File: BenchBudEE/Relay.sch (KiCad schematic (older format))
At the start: 11 parts, among them K1 1461069-5, Q1 2N3904, U1 LTV-816S

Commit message: Layout Work Session 18
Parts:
- added TP4: RELAY_LOW, symbol CONN_1
- added TP?: 12P, symbol CONN_1
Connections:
- net +12P: now also TP?.1
- net at D2.1 (A), K1.5 (COIL-), Q1.3 (C): now also TP4.1
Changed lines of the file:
@@
 Sheet 5 9
 Title ""
-Date "18 mar 2014"
+Date "20 mar 2014"
 Rev ""
 Comp ""
@@
 	6500 1700 6500 1350
 $Comp
-L +12P #PWR038
+L +12P #PWR44
 U 1 1 52F63026
 P 6500 1350
-F 0 "#PWR038" H 6500 1320 30  0001 C CNN
+F 0 "#PWR44" H 6500 1320 30  0001 C CNN
 F 1 "+12P" H 6500 1450 30  0000 C CNN
 F 2 "" H 6500 1350 60  0000 C CNN
@@
 	7650 1750 7650 1400
 Wire Wire Line
-	7650 1400 6500 1400
+	6500 1400 7850 1400
 Connection ~ 6500 1400
 $Comp
-L GND_RELAY #PWR039
+L GND_RELAY #PWR45
 U 1 1 53133457
 P 8300 4800
-F 0 "#PWR039" H 8300 4800 30  0001 C CNN
+F 0 "#PWR45" H 8300 4800 30  0001 C CNN
 F 1 "GND_RELAY" H 8300 4730 30  0000 C CNN
 F 2 "" H 8300 4800 60  0000 C CNN
@@
 	1    0    0    -1
 $EndComp
+$Comp
+L CONN_1 TP4
+U 1 1 532B3F5C
+P 8600 3250
+F 0 "TP4" H 8680 3250 40  0000 L CNN
+F 1 "RELAY_LOW" H 8600 3305 30  0001 C CNN
+F 2 "" H 8600 3250 60  0000 C CNN
+F 3 "" H 8600 3250 60  0000 C CNN
+	1    8600 3250
+	1    0    0    -1
+$EndComp
+Connection ~ 7650 2500
+Wire Wire Line
+	8450 3250 8300 3250
+Connection ~ 8300 3250
+$Comp
+L CONN_1 TP?
+U 1 1 532B6892
+P 8000 1400
+F 0 "TP?" H 8080 1400 40  0000 L CNN
+F 1 "12P" H 8000 1455 30  0001 C CNN
+F 2 "" H 8000 1400 60  0000 C CNN
+F 3 "" H 8000 1400 60  0000 C CNN
+	1    8000 1400
+	1    0    0    -1
+$EndComp
+Connection ~ 7650 1400
 $EndSCHEMATC

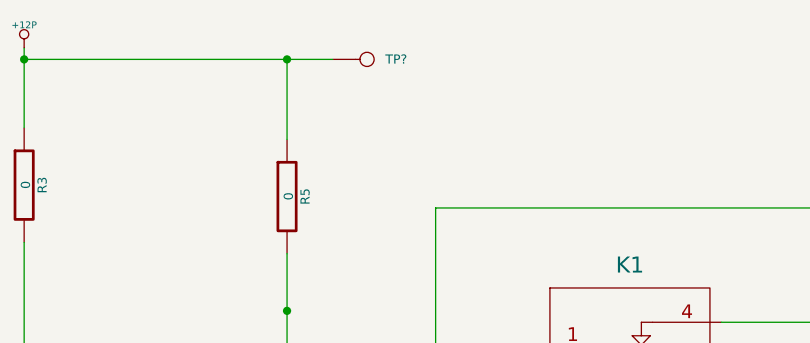
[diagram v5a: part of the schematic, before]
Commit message: Analog IO Cleanup/Additions
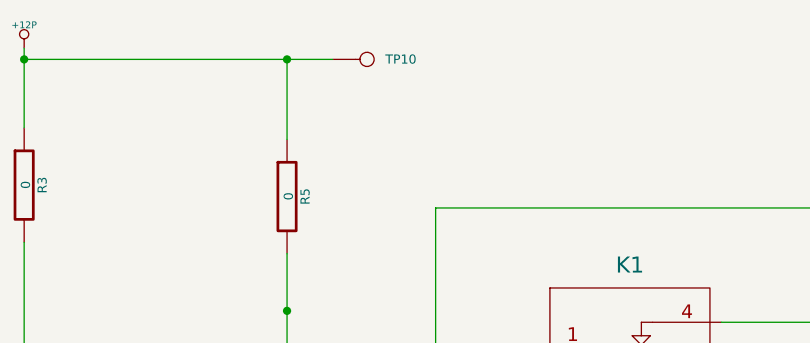
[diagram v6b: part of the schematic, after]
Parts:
- gave numbers to parts that had none: 1
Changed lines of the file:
@@
 Sheet 5 9
 Title ""
-Date "20 mar 2014"
+Date "26 mar 2014"
 Rev ""
 Comp ""
@@
 	6500 1700 6500 1350
 $Comp
-L +12P #PWR44
+L +12P #PWR037
 U 1 1 52F63026
 P 6500 1350
-F 0 "#PWR44" H 6500 1320 30  0001 C CNN
+F 0 "#PWR037" H 6500 1320 30  0001 C CNN
 F 1 "+12P" H 6500 1450 30  0000 C CNN
 F 2 "" H 6500 1350 60  0000 C CNN
@@
 Connection ~ 6500 1400
 $Comp
-L GND_RELAY #PWR45
+L GND_RELAY #PWR038
 U 1 1 53133457
 P 8300 4800
-F 0 "#PWR45" H 8300 4800 30  0001 C CNN
+F 0 "#PWR038" H 8300 4800 30  0001 C CNN
 F 1 "GND_RELAY" H 8300 4730 30  0000 C CNN
 F 2 "" H 8300 4800 60  0000 C CNN
@@
 Connection ~ 8300 3250
 $Comp
-L CONN_1 TP?
+L CONN_1 TP10
 U 1 1 532B6892
 P 8000 1400
-F 0 "TP?" H 8080 1400 40  0000 L CNN
+F 0 "TP10" H 8080 1400 40  0000 L CNN
 F 1 "12P" H 8000 1455 30  0001 C CNN
 F 2 "" H 8000 1400 60  0000 C CNN

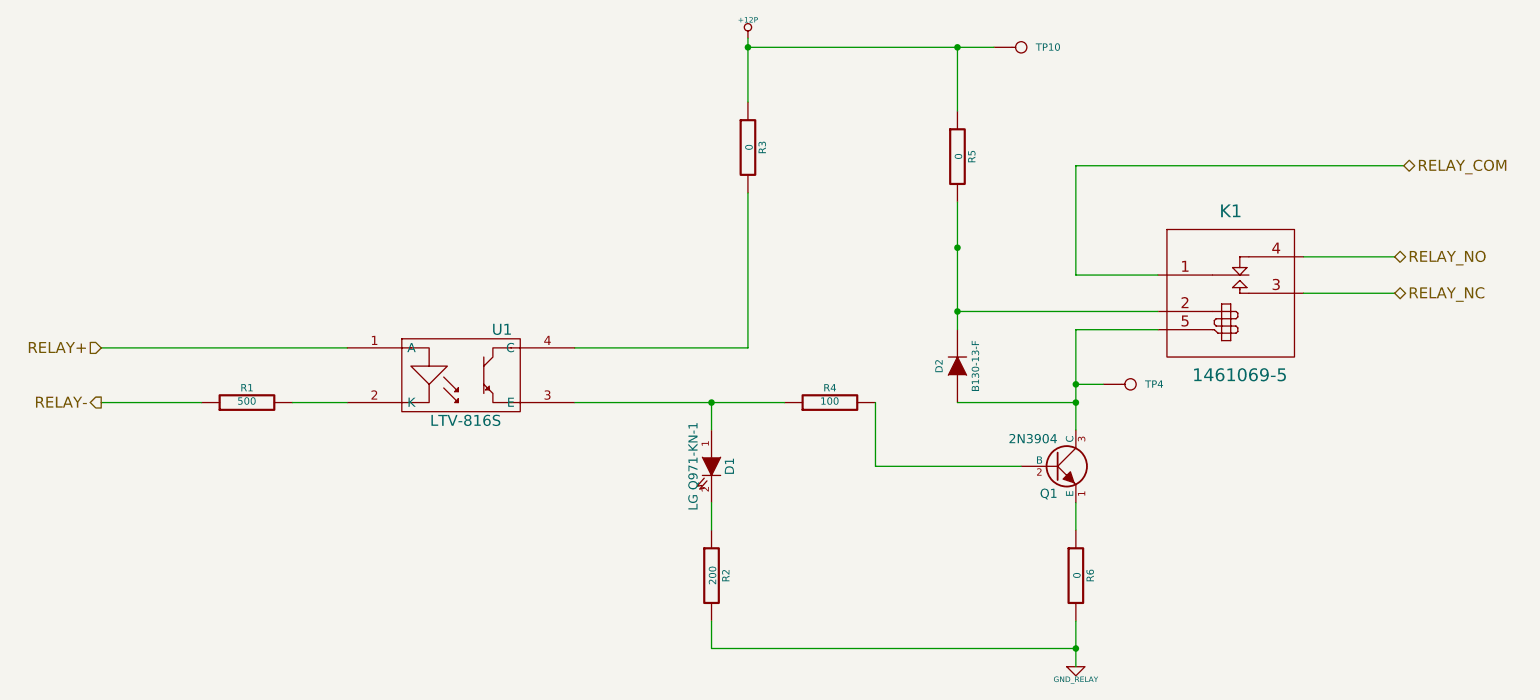
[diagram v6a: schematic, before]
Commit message: Changes for the BOM and BOMs
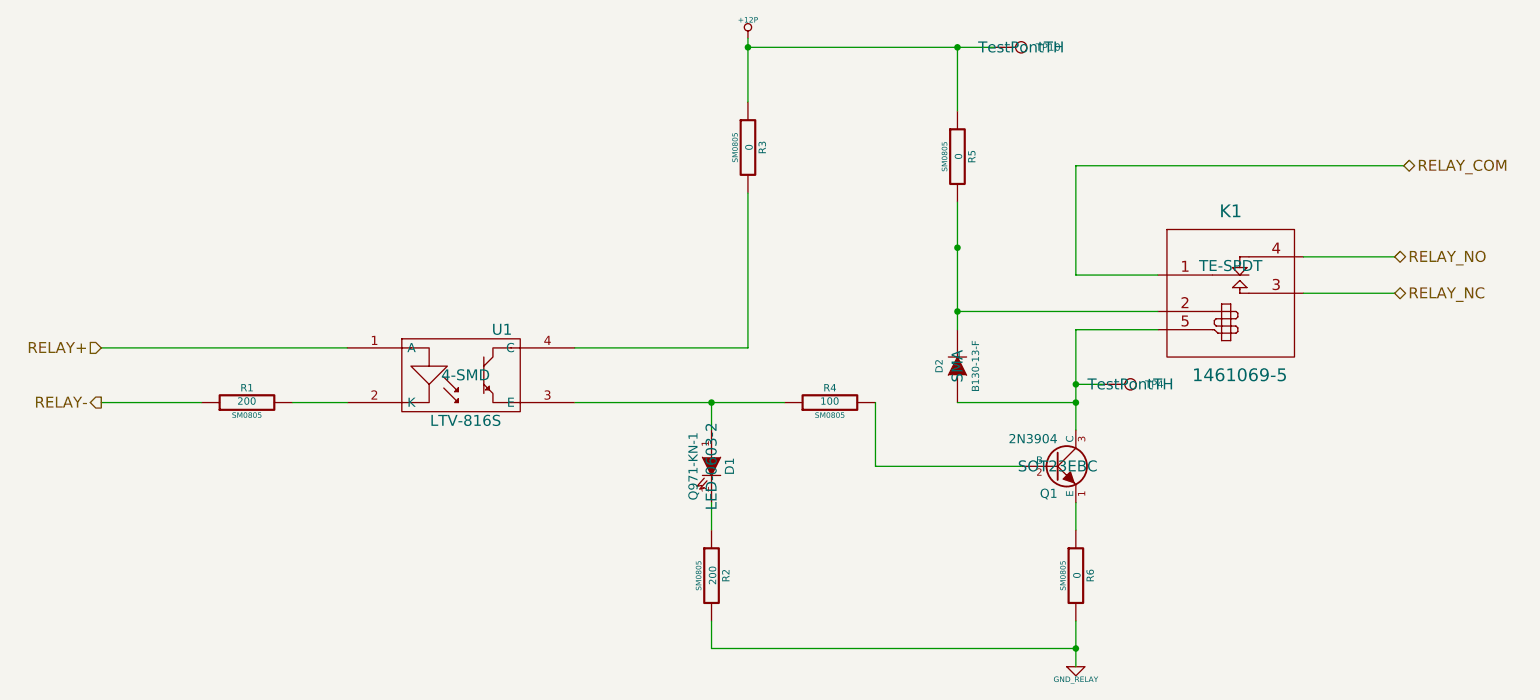
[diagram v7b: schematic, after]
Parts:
- D1: value LG Q971-KN-1 -> Q971-KN-1; footprint ~ -> LED-0603-2
- D2: footprint ~ -> SMA
- K1: footprint ~ -> TE-SPDT
- Q1: footprint ~ -> SOT23EBC
- R1: value 500 -> 200; footprint ~ -> SM0805
- R2, R3, R4, R5, R6: footprint ~ -> SM0805
- TP10, TP4: footprint (none) -> TestPontTH
- U1: footprint (none) -> 4-SMD
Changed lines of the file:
@@
 Sheet 5 9
 Title ""
-Date "26 mar 2014"
+Date "26 apr 2014"
 Rev ""
 Comp ""
@@
 F 0 "R6" V 8380 4300 40  0000 C CNN
 F 1 "0" V 8307 4301 40  0000 C CNN
-F 2 "~" V 8230 4300 30  0000 C CNN
+F 2 "SM0805" V 8230 4300 30  0000 C CNN
 F 3 "~" H 8300 4300 30  0000 C CNN
 	1    8300 4300
@@
 F 0 "Q1" H 8200 3550 50  0000 R CNN
 F 1 "2N3904" H 8200 3850 50  0000 R CNN
-F 2 "~" H 8200 3700 60  0000 C CNN
+F 2 "SOT23EBC" H 8200 3700 60  0000 C CNN
 F 3 "~" H 8200 3700 60  0000 C CNN
 F 4 "Diodes Inc" H 8200 3700 60  0001 C CNN "MFG Name"
@@
 P 6300 3700
 F 0 "D1" H 6300 3800 50  0000 C CNN
-F 1 "LG Q971-KN-1" H 6300 3600 50  0000 C CNN
-F 2 "~" H 6300 3700 60  0000 C CNN
+F 1 "Q971-KN-1" H 6300 3600 50  0000 C CNN
+F 2 "LED-0603-2" H 6300 3700 60  0000 C CNN
 F 3 "~" H 6300 3700 60  0000 C CNN
 	1    6300 3700
@@
 F 0 "K1" H 9150 2900 70  0000 C CNN
 F 1 "1461069-5" H 9200 2000 70  0000 C CNN
-F 2 "~" H 9150 2600 60  0000 C CNN
+F 2 "TE-SPDT" H 9150 2600 60  0000 C CNN
 F 3 "~" H 9150 2600 60  0000 C CNN
 	1    9150 2600
@@
 F 0 "R2" V 6380 4300 40  0000 C CNN
 F 1 "200" V 6307 4301 40  0000 C CNN
-F 2 "~" V 6230 4300 30  0000 C CNN
+F 2 "SM0805" V 6230 4300 30  0000 C CNN
 F 3 "~" H 6300 4300 30  0000 C CNN
 	1    6300 4300
@@
 F 0 "R4" V 7030 3350 40  0000 C CNN
 F 1 "100" V 6957 3351 40  0000 C CNN
-F 2 "~" V 6880 3350 30  0000 C CNN
+F 2 "SM0805" V 6880 3350 30  0000 C CNN
 F 3 "~" H 6950 3350 30  0000 C CNN
 	1    6950 3350
@@
 F 0 "R3" V 6580 1950 40  0000 C CNN
 F 1 "0" V 6507 1951 40  0000 C CNN
-F 2 "~" V 6430 1950 30  0000 C CNN
+F 2 "SM0805" V 6430 1950 30  0000 C CNN
 F 3 "~" H 6500 1950 30  0000 C CNN
 	1    6500 1950
@@
 P 3750 3350
 F 0 "R1" V 3830 3350 40  0000 C CNN
-F 1 "500" V 3757 3351 40  0000 C CNN
-F 2 "~" V 3680 3350 30  0000 C CNN
+F 1 "200" V 3757 3351 40  0000 C CNN
+F 2 "SM0805" V 3680 3350 30  0000 C CNN
 F 3 "~" H 3750 3350 30  0000 C CNN
 	1    3750 3350
@@
 F 0 "D2" H 7650 3250 40  0000 C CNN
 F 1 "B130-13-F" H 7650 3050 40  0000 C CNN
-F 2 "~" H 7650 3150 60  0000 C CNN
+F 2 "SMA" H 7650 3150 60  0000 C CNN
 F 3 "~" H 7650 3150 60  0000 C CNN
 	1    7650 3150
@@
 F 0 "U1" H 5150 3450 60  0000 C CNN
 F 1 "LTV-816S" H 4950 2950 60  0000 C CNN
-F 2 "" H 4950 3200 60  0000 C CNN
+F 2 "4-SMD" H 4950 3200 60  0000 C CNN
 F 3 "" H 4950 3200 60  0000 C CNN
 F 4 "LTV-816S" H 4950 3200 60  0001 C CNN "MFG Part Number"
@@
 F 0 "R5" V 7730 2000 40  0000 C CNN
 F 1 "0" V 7657 2001 40  0000 C CNN
-F 2 "~" V 7580 2000 30  0000 C CNN
+F 2 "SM0805" V 7580 2000 30  0000 C CNN
 F 3 "~" H 7650 2000 30  0000 C CNN
 	1    7650 2000
@@
 F 0 "TP4" H 8680 3250 40  0000 L CNN
 F 1 "RELAY_LOW" H 8600 3305 30  0001 C CNN
-F 2 "" H 8600 3250 60  0000 C CNN
+F 2 "TestPontTH" H 8600 3250 60  0000 C CNN
 F 3 "" H 8600 3250 60  0000 C CNN
 	1    8600 3250
@@
 F 0 "TP10" H 8080 1400 40  0000 L CNN
 F 1 "12P" H 8000 1455 30  0001 C CNN
-F 2 "" H 8000 1400 60  0000 C CNN
+F 2 "TestPontTH" H 8000 1400 60  0000 C CNN
 F 3 "" H 8000 1400 60  0000 C CNN
 	1    8000 1400
